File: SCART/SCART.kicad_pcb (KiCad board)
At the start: 2 copper layers, 67.4 x 96.4 mm, 2 parts, among them J2 Ground, J3 Breakout

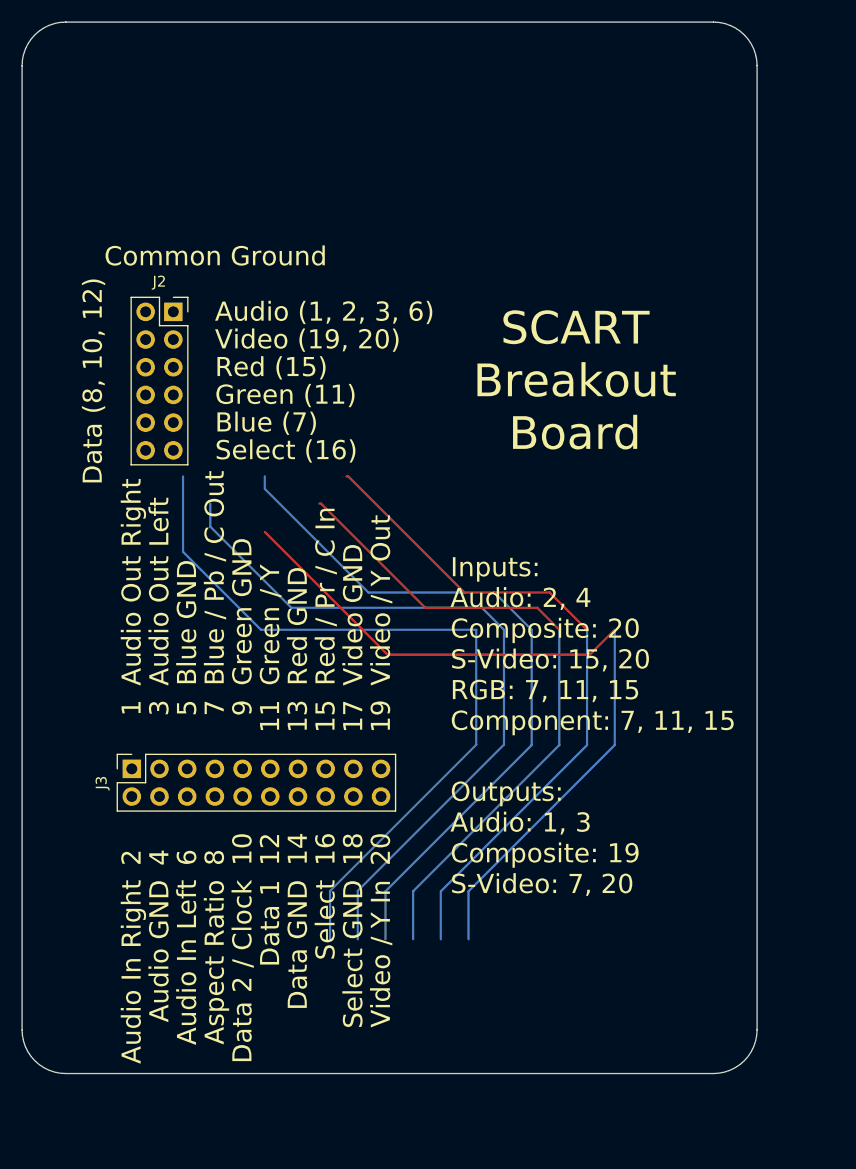
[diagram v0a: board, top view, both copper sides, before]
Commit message: Finish SCART board.
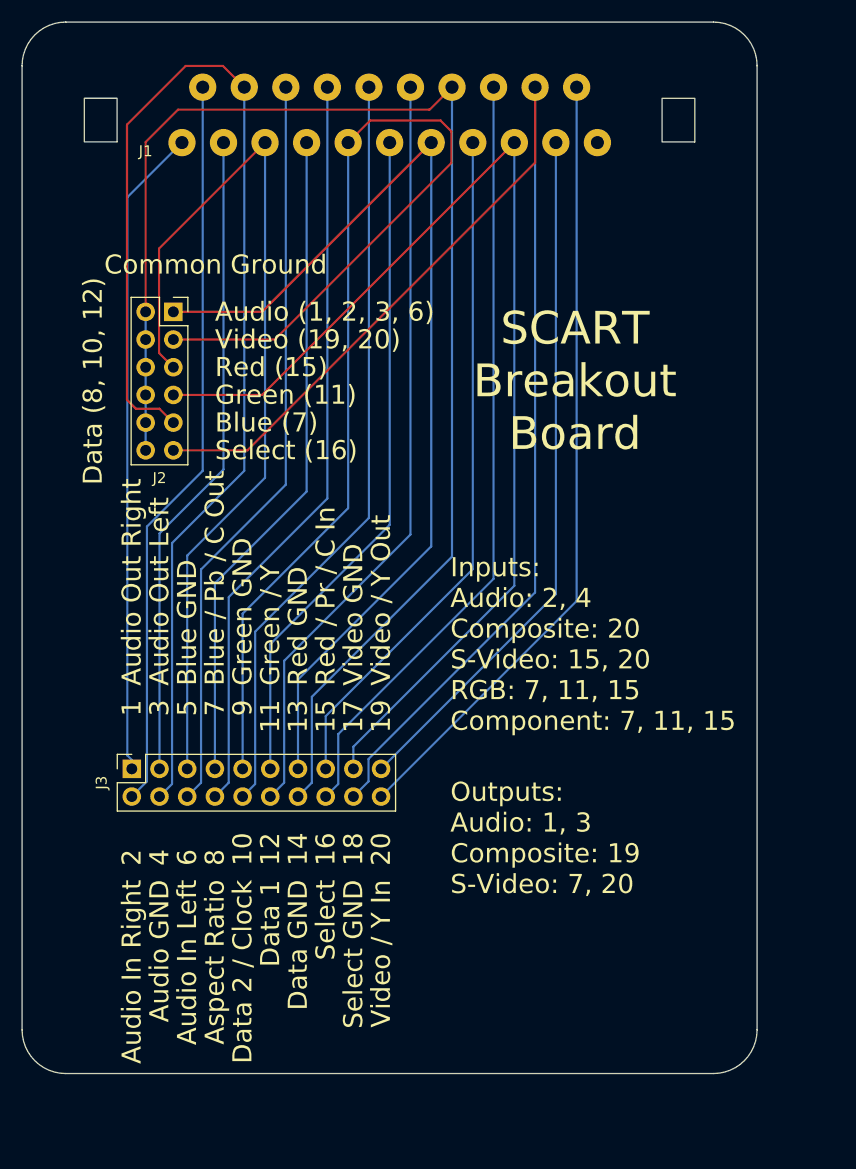
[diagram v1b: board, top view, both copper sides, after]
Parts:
- added J1: Socket, T-Pau:SCART, F.Cu at (99.8, 35.3)
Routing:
- net /Data GND: track 0.00 -> 129.3 mm
- net /Blanking GND: track 0.00 -> 123.0 mm
- net /Audio GND: track 0.00 -> 112.4 mm
- net /Composite GND: track 0.00 -> 104.4 mm
- net /RGB Red GND: track 0.00 -> 92.6 mm
- net (no net): track 92.4 -> 0.00 mm
- net /RGB Green GND: track 33.9 -> 107.3 mm
- net /Blanking: track 0.00 -> 71.4 mm
- net /Data 1: track 0.00 -> 70.4 mm
- net /Data 2: track 0.00 -> 69.8 mm
- net /Status: track 0.00 -> 69.3 mm
- net /Audio In Left: track 0.00 -> 68.8 mm
- net /Audio In Right: track 0.00 -> 67.7 mm
- net /Composite Out: track 0.00 -> 64.1 mm
- net /RGB Red: track 0.00 -> 63.0 mm
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
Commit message: Adapt to fixed footprint.
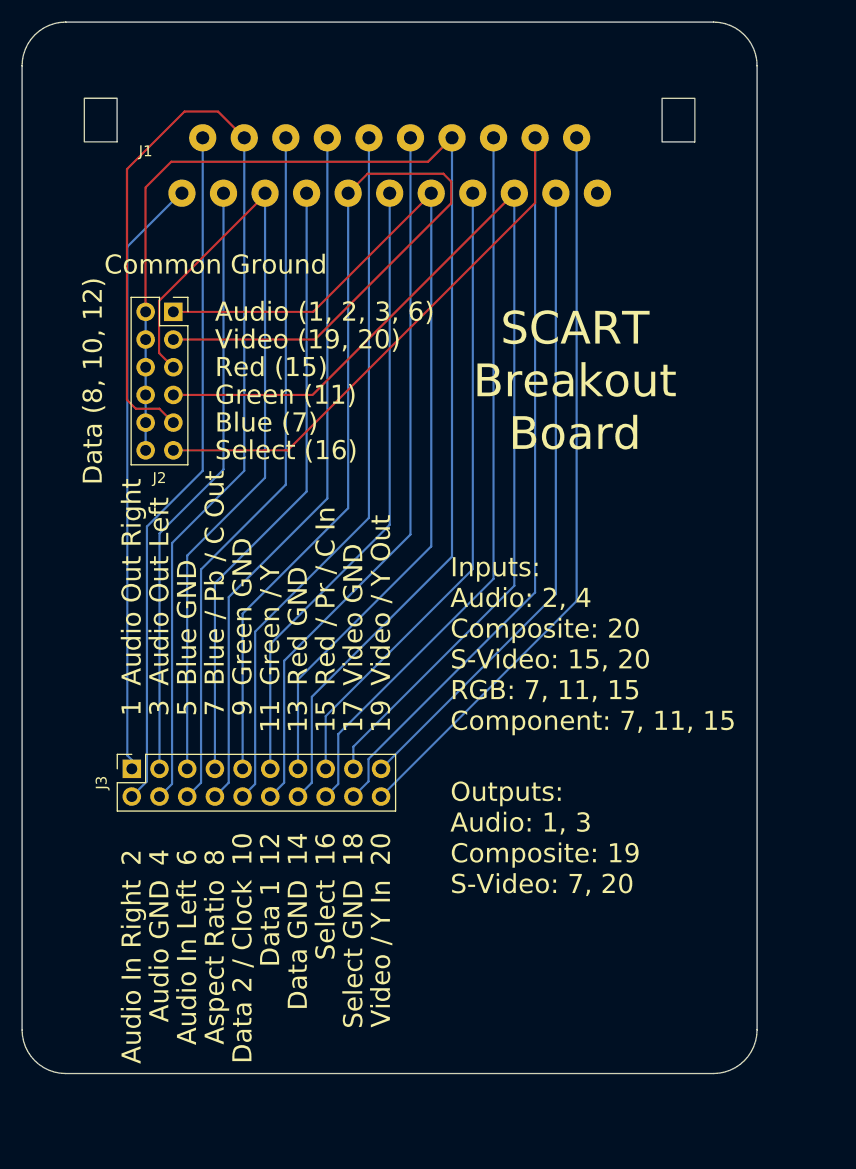
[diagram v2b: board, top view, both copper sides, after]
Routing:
- net /RGB Blue GND: track 85.6 -> 76.3 mm
- net /Data GND: track 129.3 -> 120.4 mm
- net /Audio GND: track 112.4 -> 103.8 mm
- net /RGB Green GND: track 107.3 -> 100.0 mm
- net /Blanking GND: track 123.0 -> 116.0 mm
- net /RGB Red GND: track 92.6 -> 86.0 mm
- net /Composite GND: track 104.4 -> 97.9 mm
- net /Data 2: track 69.8 -> 65.2 mm
- net /RGB Blue: track 60.9 -> 56.2 mm
- net /Audio In Right: track 67.7 -> 63.1 mm
- net /Status: track 69.3 -> 64.7 mm
- net /Data 1: track 70.4 -> 65.8 mm
- net /Blanking: track 71.4 -> 66.8 mm
- net /RGB Red: track 63.0 -> 58.4 mm
- net /Audio In Left: track 68.8 -> 64.2 mm
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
